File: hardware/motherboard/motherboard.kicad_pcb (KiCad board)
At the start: 4 copper layers, 180.3 x 281.9 mm, 54 parts, among them J1 DB37_Female, J10 DB37_Female, J11 DB37_Female, J12 Barrel_Jack, J13 TSR 1-2433, J2 DB37_Female, J3 DB37_Female, J4 DB37_Female, J5 DB37_Female, J6 DB25_Female, J7 DB37_Female, J8 DB25_Female, J9 DB9_Female, SW1 SW_SPST, U1 SN74ALVC00, U10 SN74ALVC00, U11 SN74ALVC00, U12 SN74ALVC00, U13 SN74ALVC00, U14 SN74ALVC00, U15 SN74ALVC00, U16 SN74ALVC00, U17 SN74ALVC00, U18 SN74ALVC00, U19 SN74ALVC00, U2 SN74ALVC00, U20 SN74ALVC00, U21 SN74ALVC00, U22 SN74ALVC00, U23 SN74ALVC00, U24 SN74ALVC00, U25 SN74ALVC00, U26 SN74ALVC00, U27 SN74ALVC00, U28 SN74ALVC00, U29 SN74ALVC00, U3 SN74ALVC00, U30 SN74ALVC00, U31 SN74ALVC00, U32 SN74ALVC00, U4 SN74ALVC00, U5 SN74ALVC00, U6 SN74ALVC00, U7 SN74ALVC00, U8 SN74ALVC00, U9 SN74ALVC00

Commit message: All boards as fabbed at v1.0
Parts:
- added D1: LED, LED_SMD:LED_1206_3216Metric, F.Cu at (429.9, 108.6)
- added D10: LED, LED_SMD:LED_1206_3216Metric, F.Cu at (389.9, 108.6)
- added D11: LED, LED_SMD:LED_1206_3216Metric, F.Cu at (385.4, 108.6)
- added D12: LED, LED_SMD:LED_1206_3216Metric, F.Cu at (381.0, 108.6)
- added D13: LED, LED_SMD:LED_1206_3216Metric, F.Cu at (376.6, 108.6)
- added D14: LED, LED_SMD:LED_1206_3216Metric, F.Cu at (372.1, 108.6)
- added D15: LED, LED_SMD:LED_1206_3216Metric, F.Cu at (367.7, 108.6)
- added D16: LED, LED_SMD:LED_1206_3216Metric, F.Cu at (361.3, 103.5)
- added D17: LED, LED_SMD:LED_1206_3216Metric, F.Cu at (361.3, 113.7)
- added D2: LED, LED_SMD:LED_1206_3216Metric, F.Cu at (425.4, 108.6)
- added D3: LED, LED_SMD:LED_1206_3216Metric, F.Cu at (421.0, 108.6)
- added D4: LED, LED_SMD:LED_1206_3216Metric, F.Cu at (416.6, 108.6)
- added D5: LED, LED_SMD:LED_1206_3216Metric, F.Cu at (412.1, 108.6)
- added D6: LED, LED_SMD:LED_1206_3216Metric, F.Cu at (407.7, 108.6)
- added D7: LED, LED_SMD:LED_1206_3216Metric, F.Cu at (403.2, 108.6)
- added D8: LED, LED_SMD:LED_1206_3216Metric, F.Cu at (398.8, 108.6)
- added D9: LED, LED_SMD:LED_1206_3216Metric, F.Cu at (394.3, 108.6)
- added R10: 1K, Resistor_SMD:R_1206_3216Metric, F.Cu at (398.8, 92.1)
- added R11: 1K, Resistor_SMD:R_1206_3216Metric, F.Cu at (394.3, 92.1)
- added R12: 1K, Resistor_SMD:R_1206_3216Metric, F.Cu at (389.9, 92.1)
- added R13: 1K, Resistor_SMD:R_1206_3216Metric, F.Cu at (385.4, 92.1)
- added R14: 1K, Resistor_SMD:R_1206_3216Metric, F.Cu at (381.0, 92.1)
- added R15: 1K, Resistor_SMD:R_1206_3216Metric, F.Cu at (376.6, 92.1)
- added R16: 1K, Resistor_SMD:R_1206_3216Metric, F.Cu at (372.1, 92.1)
- added R17: 1K, Resistor_SMD:R_1206_3216Metric, F.Cu at (367.7, 92.1)
- added R18: 1K, Resistor_SMD:R_1206_3216Metric, F.Cu at (357.5, 103.5)
- added R19: 1K, Resistor_SMD:R_1206_3216Metric, F.Cu at (357.5, 113.7)
- added R3: 1K, Resistor_SMD:R_1206_3216Metric, F.Cu at (429.9, 92.1)
- added R4: 1K, Resistor_SMD:R_1206_3216Metric, F.Cu at (425.4, 92.1)
- added R5: 1K, Resistor_SMD:R_1206_3216Metric, F.Cu at (421.0, 92.1)
- added R6: 1K, Resistor_SMD:R_1206_3216Metric, F.Cu at (416.6, 92.1)
- added R7: 1K, Resistor_SMD:R_1206_3216Metric, F.Cu at (412.1, 92.1)
- added R8: 1K, Resistor_SMD:R_1206_3216Metric, F.Cu at (407.7, 92.1)
- added R9: 1K, Resistor_SMD:R_1206_3216Metric, F.Cu at (403.2, 92.1)
- moved G*** 12.2 mm to (395.0, 176.5)
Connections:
- net /sheet5EAF90EF/not_sel renamed ~inst_15
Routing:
- net ~inst_15: track 172.1 -> 266.7 mm, vias 12 -> 13
- net inst_0: track 427.3 -> 498.4 mm, vias 4 -> 5
- net inst_1: track 429.1 -> 492.7 mm, vias 4 -> 5
- net inst_2: track 427.9 -> 485.8 mm, vias 4 -> 5
- net inst_3: track 401.5 -> 453.3 mm, vias 4 -> 5
- net inst_4: track 458.5 -> 504.1 mm, vias 4 -> 5
- net inst_5: track 451.2 -> 490.3 mm, vias 4 -> 5
- net inst_6: track 433.9 -> 467.4 mm, vias 3 -> 4
- net inst_15: track 762.4 -> 790.2 mm, vias 21 -> 22
- net inst_7: track 431.2 -> 458.9 mm, vias 2 -> 3
- net inst_14: track 362.2 -> 386.5 mm, vias 2 -> 3
- net inst_8: track 432.9 -> 454.4 mm, vias 3 -> 4
- net inst_9: track 425.0 -> 440.1 mm, vias 3 -> 4
- net Net-(D9-Pad1): track 0.00 -> 13.7 mm
- net Net-(D8-Pad1): track 0.00 -> 13.7 mm
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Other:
- board text added: "!out"
- board text added: "!x"
- board text added: "!y"
- board text added: "0"
- board text added: "1"
- board text added: "10"
- board text added: "11"
- board text added: "12"
- board text added: "13"
- board text added: "14"
- board text added: "2"
- board text added: "3"
- board text added: "4"
- board text added: "5"
- board text added: "6"
- board text added: "7"
- board text added: "8"
- board text added: "9"
- board text added: "<0"
- board text added: "=0"
- board text added: ">0"
- board text added: "A"
- board text added: "A-inst"
- board text added: "C-inst"
- board text added: "D"
- board text added: "M"
- board text added: "compute"
- board text added: "dest"
- board text added: "jump"
- board text added: "x+y x&y"
- board text added: "x=M x=A"
- board text added: "zx"
- board text added: "zy"

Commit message: Motherboard: Added power switch, moved reset switch, modified silkscreens for readability, fixed A-register connector pinout, grounded NC input pins, changed paste layer clearance to -0.05mm
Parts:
- added SW2: SW_SPST, nandirl logo:SPST Toggle Switch, F.Cu at (378.5, 266.7)
- moved R2 61.0 mm to (397.4, 263.4)
- moved SW1 61.0 mm to (389.6, 263.9)
- moved G*** 1.80 mm to (395.2, 174.8)
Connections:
- C1 pad 1: Vin -> Net-(C1-Pad1)
- J1 pad 1: areg_in15 -> areg_out0
- J1 pad 11: areg_out1 -> areg_in14
- J1 pad 12: areg_out3 -> areg_in12
- J1 pad 13: areg_out5 -> areg_in10
- J1 pad 14: areg_out7 -> areg_in8
- J1 pad 15: areg_out9 -> areg_in6
- J1 pad 16: areg_out11 -> areg_in4
- J1 pad 17: areg_out13 -> areg_in2
- J1 pad 18: areg_out15 -> areg_in0
- J1 pad 2: areg_in13 -> areg_out2
- J1 pad 20: areg_in14 -> areg_out1
- J1 pad 21: areg_in12 -> areg_out3
- J1 pad 22: areg_in10 -> areg_out5
- J1 pad 23: areg_in8 -> areg_out7
- J1 pad 24: areg_in6 -> areg_out9
- J1 pad 25: areg_in4 -> areg_out11
- J1 pad 26: areg_in2 -> areg_out13
- J1 pad 27: areg_in0 -> areg_out15
- J1 pad 29: areg_out0 -> areg_in15
- J1 pad 3: areg_in11 -> areg_out4
- J1 pad 30: areg_out2 -> areg_in13
- J1 pad 31: areg_out4 -> areg_in11
- J1 pad 32: areg_out6 -> areg_in9
- J1 pad 33: areg_out8 -> areg_in7
- J1 pad 34: areg_out10 -> areg_in5
- J1 pad 35: areg_out12 -> areg_in3
- J1 pad 36: areg_out14 -> areg_in1
- J1 pad 4: areg_in9 -> areg_out6
- J1 pad 5: areg_in7 -> areg_out8
- J1 pad 6: areg_in5 -> areg_out10
- J1 pad 7: areg_in3 -> areg_out12
- J1 pad 8: areg_in1 -> areg_out14
- J12 pad 1: Vin -> Net-(C1-Pad1)
- U13 pad 10: Net-(U13-Pad10) -> GND
- U13 pad 12: Net-(U13-Pad12) -> GND
- U13 pad 13: Net-(U13-Pad13) -> GND
- U13 pad 4: Net-(U13-Pad4) -> GND
- U13 pad 5: Net-(U13-Pad5) -> GND
- U13 pad 9: Net-(U13-Pad9) -> GND
- U26 pad 10: Net-(U26-Pad10) -> GND
- U26 pad 12: Net-(U26-Pad12) -> GND
- U26 pad 13: Net-(U26-Pad13) -> GND
- U26 pad 4: Net-(U26-Pad4) -> GND
- U26 pad 5: Net-(U26-Pad5) -> GND
- U26 pad 9: Net-(U26-Pad9) -> GND
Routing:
- net reset: track 361.5 -> 427.7 mm, vias 3 -> 4
- net areg_out15: track 210.0 -> 255.2 mm, vias 4 -> 5
- net Net-(C1-Pad1): track 0.00 -> 42.1 mm
- net areg_out1: track 287.8 -> 319.4 mm
- net areg_in13: track 27.4 -> 56.8 mm
- net areg_out7: track 242.6 -> 272.0 mm
- net areg_out5: track 249.2 -> 278.5 mm
- net areg_out3: track 263.5 -> 292.8 mm
- net areg_out13: track 263.0 -> 292.3 mm
- net areg_out11: track 255.3 -> 284.7 mm
- net areg_in11: track 41.2 -> 69.9 mm
- net areg_out9: track 241.7 -> 270.3 mm
- net areg_in15: track 55.2 -> 83.0 mm
- net areg_out0: track 288.9 -> 313.9 mm
- net areg_in12: track 28.7 -> 53.3 mm
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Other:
- board text added: "OFF"
- board text added: "ON"
- board text added: "RESET"
- board text added: "v1.1"
- board text removed: "v1.0"

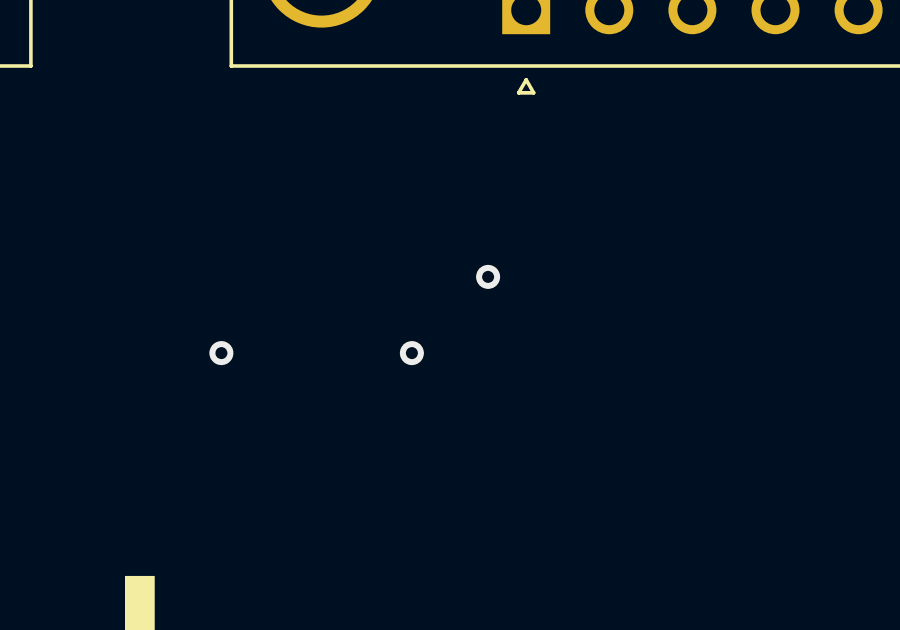
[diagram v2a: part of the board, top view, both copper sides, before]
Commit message: Debugger updated to Teensy 4.1 with magjack for ethernet. Updated motherboard<>debugger pinout to include 3.3v source
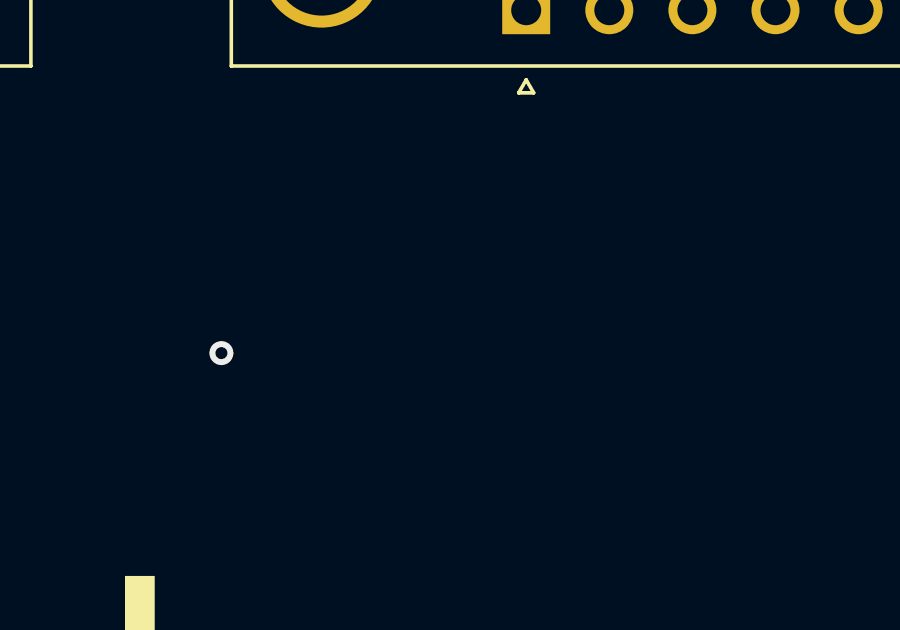
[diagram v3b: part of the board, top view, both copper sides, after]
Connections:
- J10 pad 18: rom_addr15 -> +3V3
- J10 pad 37: rom_addr16 -> +3V3
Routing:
- net rom_addr16: track 333.9 -> 0.00 mm, vias 1 -> 0
- net rom_addr15: track 327.2 -> 0.00 mm, vias 1 -> 0
